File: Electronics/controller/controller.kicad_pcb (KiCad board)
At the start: 2 copper layers, 73.7 x 61 mm, 23 parts, among them P1 POWER, P2 PANEL_1, P3 PANEL_2, P4 DIAL, P5 SWITCH, Q1 FET, U1 LM317T, U2 74HC595, U3 Arduino_Pro_Micro

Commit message: Reworking controller board.
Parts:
- removed P4: DIAL, Connect:bornier3
- removed P5: SWITCH, Connect:bornier2
- added ENC1: Encoder, Cylindric:ALPS_Encoder-EC12E2420404, F.Cu at (66.0, 92.5)
- added SW1: SW_PUSH, Discret:SW_PUSH-12mm, F.Cu at (134.6, 99.1)
- moved C1 90.6 mm to (68.6, 87.6), turned to 90 degrees
- moved C2 83.8 mm to (63.5, 85.1), turned to 270 degrees
- moved LED_DISPLAY1 83.1 mm to (100.3, 99.1), turned to 0 degrees
- moved P1 81.5 mm to (194.8, 82.3)
- moved P2 81.5 mm to (206.2, 82.3)
- moved P3 81.5 mm to (216.4, 82.3)
- moved Q1 81.5 mm to (211.3, 89.9)
- moved R2 81.5 mm to (200.5, 97.5)
- moved R3 81.5 mm to (200.5, 95.0)
- moved U1 81.5 mm to (192.9, 92.4)
- moved R8 67.0 mm to (108.0, 71.1), turned to 180 degrees
- moved R6 65.3 mm to (108.0, 73.7), turned to 180 degrees
- moved R11 63.9 mm to (108.0, 76.2), turned to 180 degrees
- moved R10 63.2 mm to (108.0, 88.9), turned to 180 degrees
- moved R5 63.0 mm to (108.0, 78.7), turned to 180 degrees
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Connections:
- LED_DISPLAY1 pad 1: /D5 -> /D15
- LED_DISPLAY1 pad 2: /D6 -> /D14
- LED_DISPLAY1 pad 6: /D7 -> /D10
- LED_DISPLAY1 pad 8: /D8 -> /D16
- U3 pad 10: /D6 -> (no net)
- U3 pad 11: /D5 -> (no net)
- U3 pad 17: (no net) -> /A0
- U3 pad 8: /D8 -> (no net)
- U3 pad 9: /D7 -> (no net)
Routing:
- net /D8: track 80.6 -> 0.00 mm
- net /D7: track 70.8 -> 0.00 mm
- net /D6: track 56.2 -> 0.00 mm
- net /D5: track 48.3 -> 0.00 mm
- net /D15: track 26.5 -> 56.9 mm
- net Net-(LED_DISPLAY1-Pad3): track 16.9 -> 42.0 mm
- net /A0: track 0.00 -> 22.9 mm
- net Net-(LED_DISPLAY1-Pad16): track 3.59 -> 25.6 mm
- net /D14: track 33.0 -> 51.8 mm
- net Net-(LED_DISPLAY1-Pad15): track 3.59 -> 22.0 mm
- net Net-(LED_DISPLAY1-Pad14): track 3.59 -> 18.4 mm
- net Net-(LED_DISPLAY1-Pad4): track 13.8 -> 26.0 mm
- net Net-(LED_DISPLAY1-Pad13): track 2.54 -> 12.3 mm
- net /D2: track 35.5 -> 28.8 mm
- net Net-(LED_DISPLAY1-Pad5): track 13.7 -> 19.9 mm
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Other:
- board outline removed

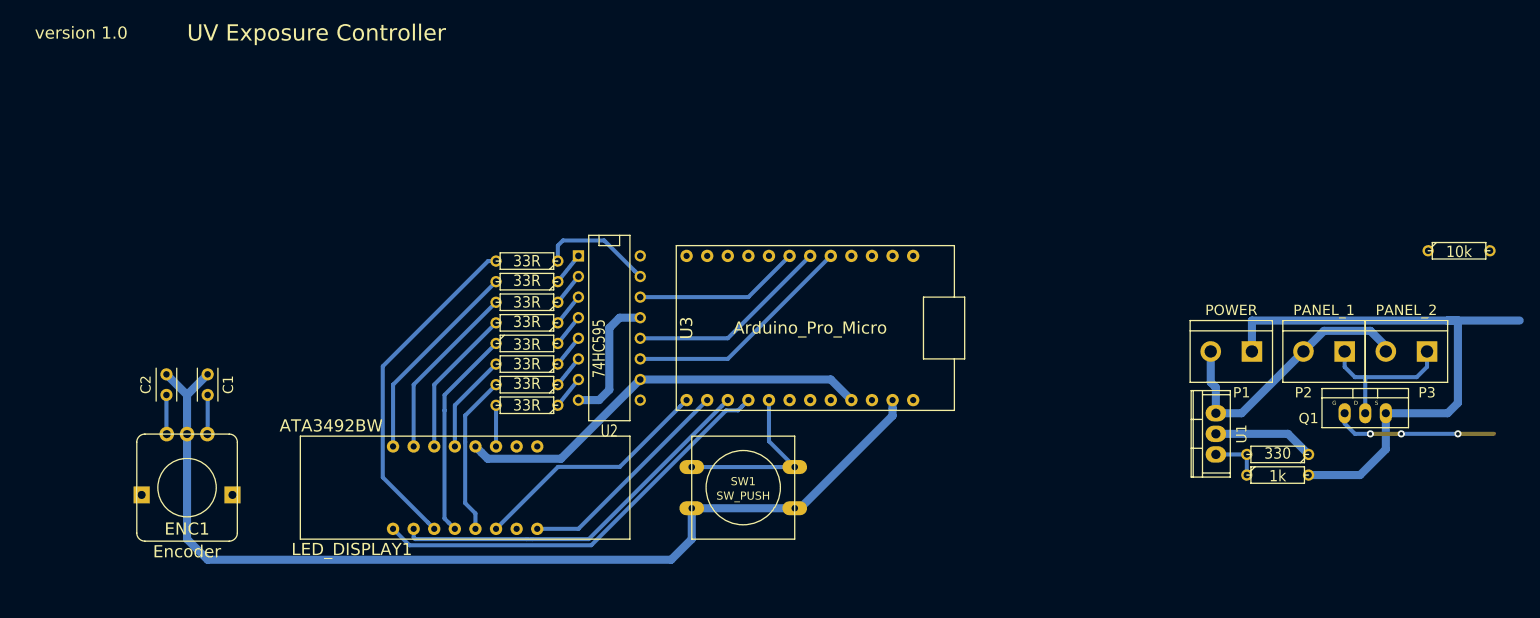
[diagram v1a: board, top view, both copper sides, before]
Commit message: Update with single layout board.
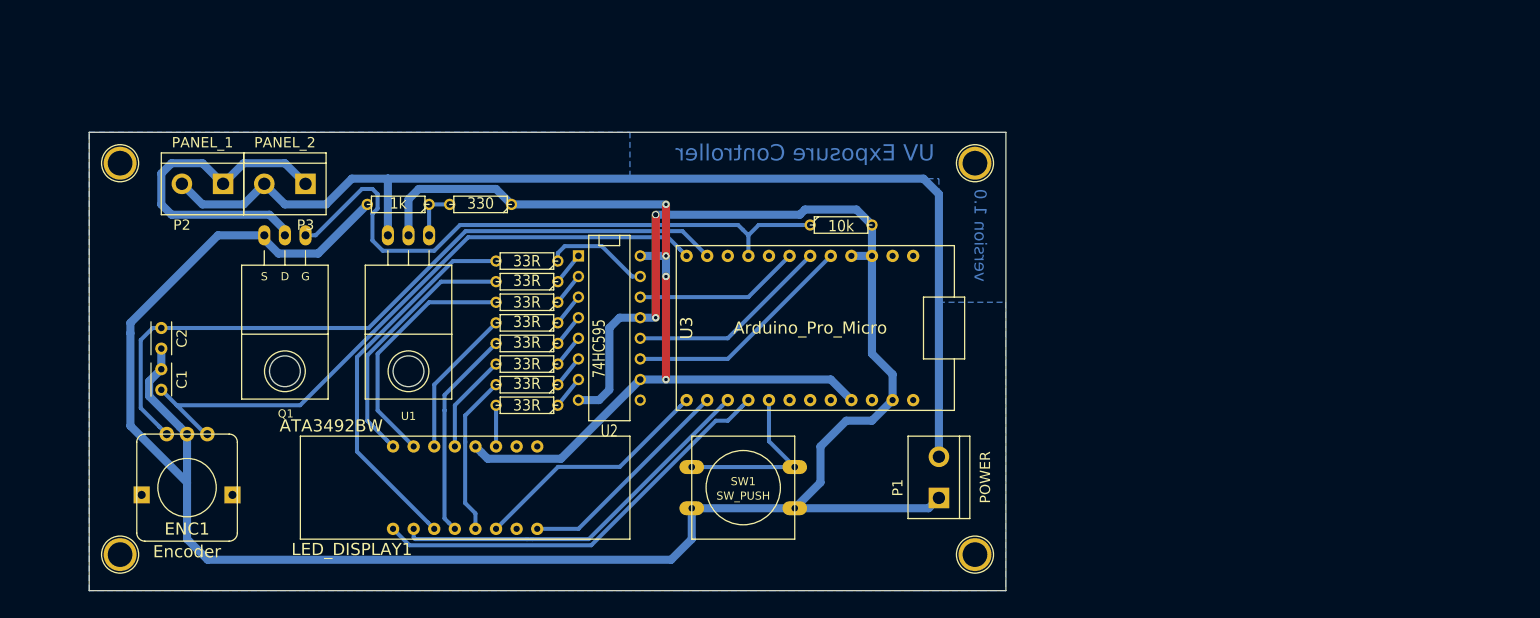
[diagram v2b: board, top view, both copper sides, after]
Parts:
- added 1pin: VAL**, Connect:1pin, F.Cu at (163.2, 59.1)
- added 1pin: VAL**, Connect:1pin, F.Cu at (163.2, 107.3)
- added 1pin: VAL**, Connect:1pin, F.Cu at (57.8, 59.1)
- added 1pin: VAL**, Connect:1pin, F.Cu at (57.8, 107.3)
- Q1: footprint Transistors_TO-220:TO-220_FET-GDS_Vertical -> Transistors_TO-220:TO-220_FET-GDS_Horizontal
- U1: footprint Power_Integrations:TO-220 -> Transistors_TO-220:TO-220_Neutral123_Horizontal
- moved P2 139.8 mm to (67.9, 61.6)
- moved P3 139.8 mm to (78.1, 61.6)
- moved Q1 135.0 mm to (78.1, 67.9), turned to 180 degrees
- moved R2 113.5 mm to (92.1, 64.1), turned to 180 degrees
- moved R3 103.0 mm to (102.2, 64.1)
- moved U1 102.5 mm to (93.3, 67.9), turned to 180 degrees
- moved R4 76.3 mm to (146.7, 66.7)
- moved P1 39.3 mm to (158.8, 97.8), turned to 90 degrees
- moved C1 5.75 mm to (62.9, 87.0)
- moved C2 3.24 mm to (62.9, 81.9), turned to 90 degrees
- turned R1 to 180 degrees
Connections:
- net Net-(P2-Pad1) renamed /12VGND
- C1 pad 1: /D14 -> /D9
- C2 pad 2: /D15 -> /D8
- ENC1 pad A: /D14 -> /D9
- ENC1 pad B: /D15 -> /D8
- Q1 pad G: /D16 -> /D6
- R1 pad 1: Net-(LED_DISPLAY1-Pad4) -> /COL
- R1 pad 2: /COL -> Net-(LED_DISPLAY1-Pad4)
- R4 pad 1: /D16 -> /D6
- U3 pad 11: (no net) -> /D8
- U3 pad 12: (no net) -> /D9
- U3 pad 9: (no net) -> /D6
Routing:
- net +12V: track 34.5 -> 138.5 mm
- net /D8: track 0.00 -> 89.7 mm
- net /D9: track 0.00 -> 80.4 mm
- net /D6: track 0.00 -> 76.9 mm
- net GND: track 215.1 -> 289.2 mm, vias 0 -> 2
- net VCC: track 64.6 -> 114.4 mm, vias 0 -> 4
- net /12VGND: track 19.5 -> 41.8 mm
- net /D16: track 47.7 -> 27.5 mm, vias 3 -> 0
- net Net-(LED_DISPLAY1-Pad15): track 22.0 -> 30.5 mm
- net Net-(LED_DISPLAY1-Pad16): track 25.6 -> 32.2 mm
- net Net-(LED_DISPLAY1-Pad3): track 42.0 -> 47.2 mm
- net /D14: track 51.8 -> 47.0 mm
- net /D15: track 56.9 -> 52.1 mm
- net /D: track 14.2 -> 13.0 mm
- added copper zone on B.Cu, net GND
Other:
- board outline added: 113 x 56.5 mm

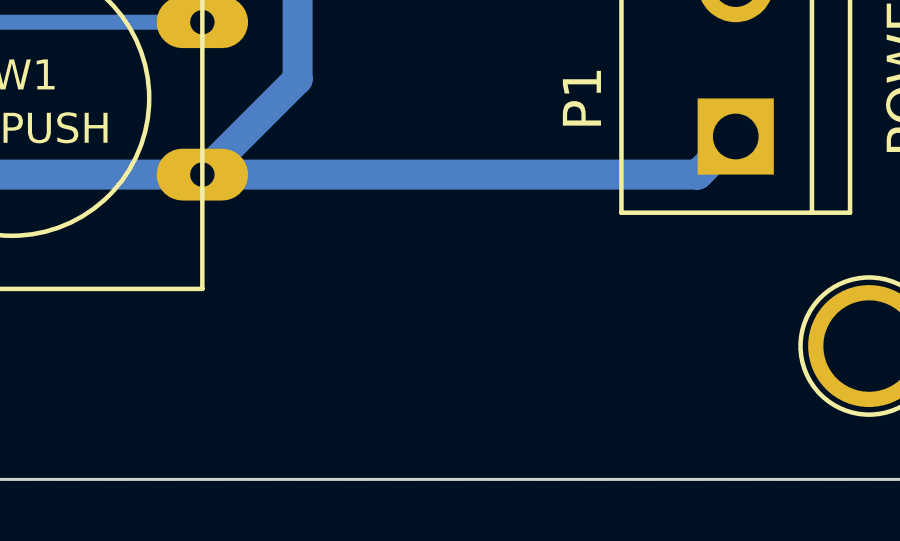
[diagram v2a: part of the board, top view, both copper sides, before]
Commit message: Added the OSHW logo to the controller.
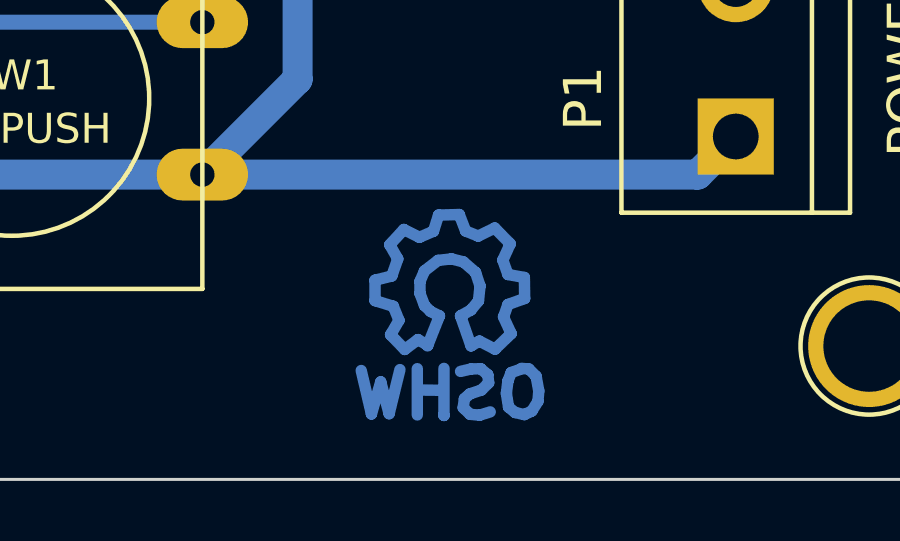
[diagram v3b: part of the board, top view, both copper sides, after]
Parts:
- added Symbol_OSHW-Logo_CopperTop: VAL**, Symbols:Symbol_OSHW-Logo_CopperTop, B.Cu at (149.2, 105.4)

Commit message: Playing with layout.
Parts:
- moved C1 6.02 mm to (68.6, 88.9)
- moved C2 4.49 mm to (63.5, 86.4), turned to 270 degrees
- moved U1 4.26 mm to (89.5, 69.8)
- moved Q1 2.29 mm to (76.8, 69.8)
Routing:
- net /D6: track 76.9 -> 87.6 mm
- net Net-(LED_DISPLAY1-Pad15): track 30.5 -> 22.0 mm
- net /D9: track 80.4 -> 72.2 mm
- net Net-(LED_DISPLAY1-Pad16): track 32.2 -> 25.6 mm
- net Net-(LED_DISPLAY1-Pad3): track 47.2 -> 41.4 mm
- net VCC: track 114.4 -> 117.8 mm
- net Net-(R2-Pad1): track 6.35 -> 9.83 mm
- net +12V: track 138.5 -> 142.0 mm
- net GND: track 289.2 -> 285.8 mm
- net /12VGND: track 41.8 -> 43.2 mm
- net /D8: track 89.7 -> 88.4 mm
- net /D15: track 52.1 -> 52.7 mm

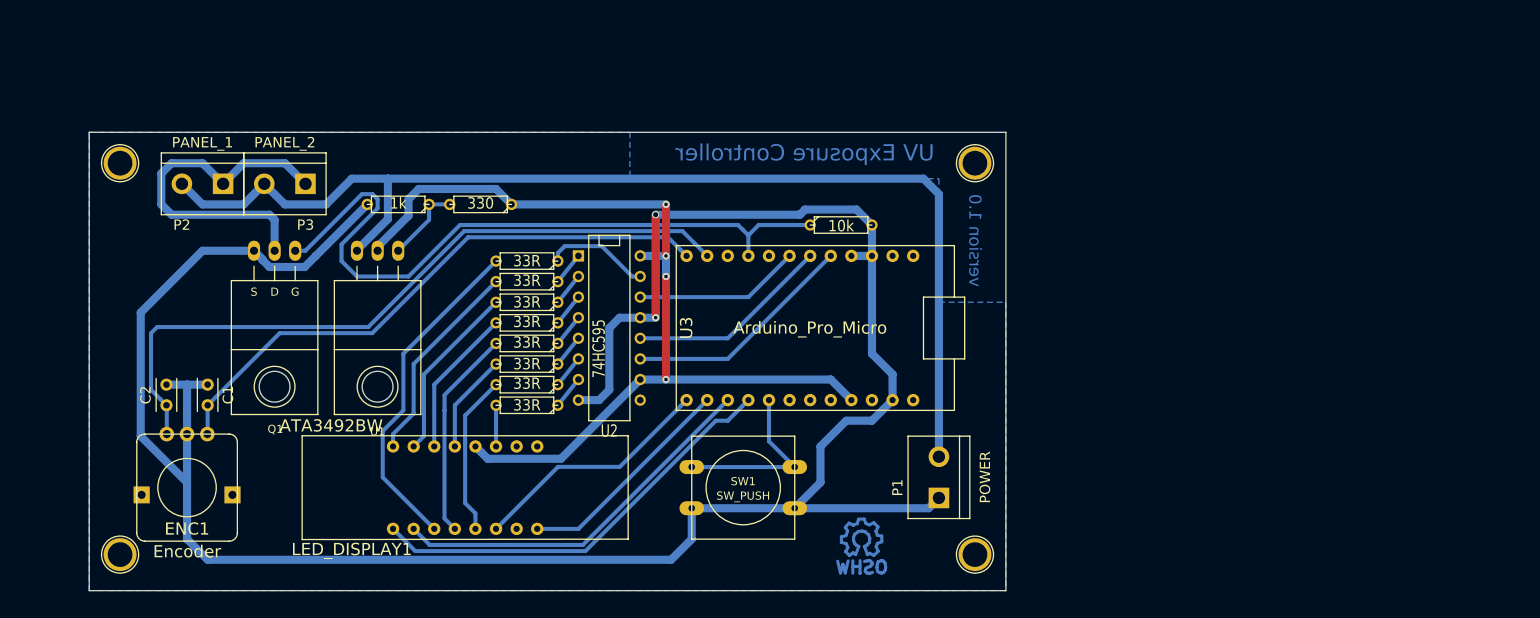
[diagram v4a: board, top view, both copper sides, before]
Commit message: Change a couple of footprints.
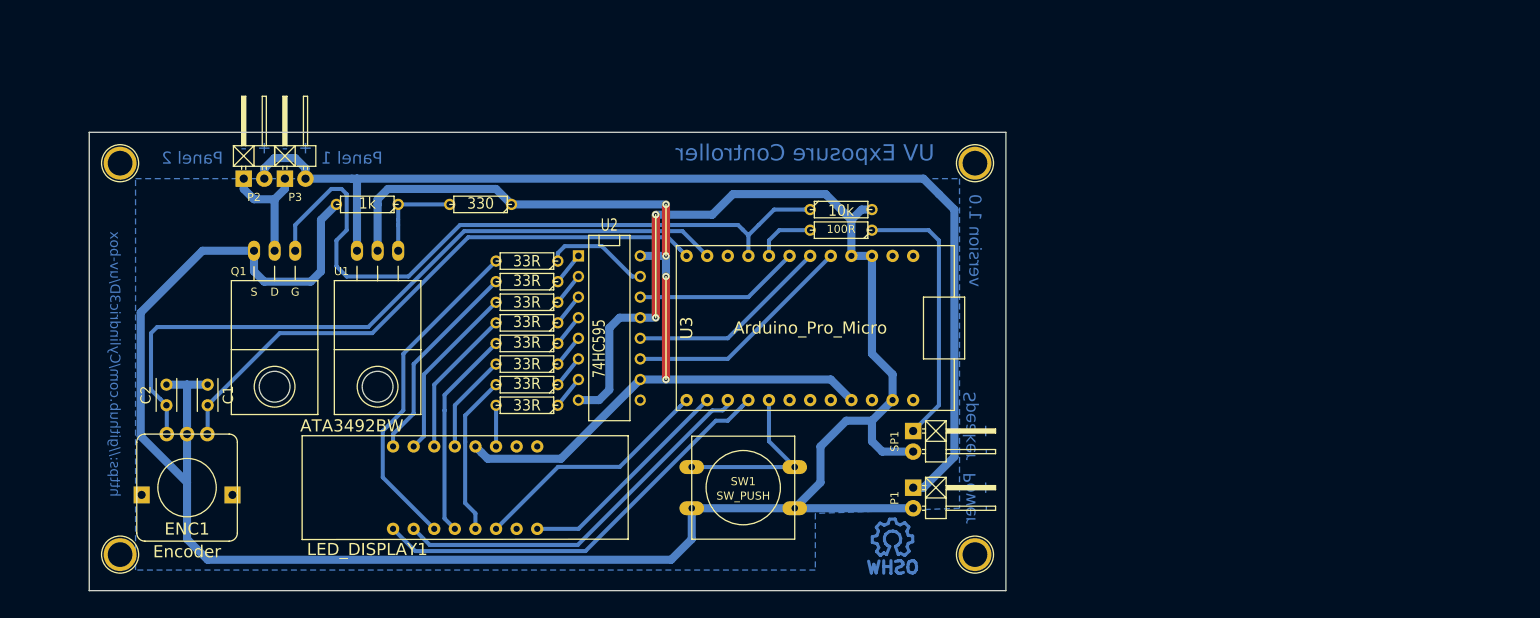
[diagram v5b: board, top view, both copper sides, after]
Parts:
- added R12: 100R, Discret:R3, F.Cu at (146.7, 67.3)
- added SP1: SPEAKER, Pin_Headers:Pin_Header_Angled_1x02, F.Cu at (155.6, 93.3)
- P1, P2, P3: footprint Connect:bornier2 -> Pin_Headers:Pin_Header_Angled_1x02
- moved P2 6.38 mm to (74.3, 61.0), turned to 0 degrees
- moved P1 4.07 mm to (155.6, 100.3), turned to 270 degrees
- moved R2 3.81 mm to (88.3, 64.1)
- moved Symbol_OSHW-Logo_CopperTop 3.81 mm to (153.0, 105.4)
- moved R4 1.91 mm to (146.7, 64.8)
- moved P3 1.42 mm to (79.4, 61.0), turned to 0 degrees
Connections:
- P1 pad 1: GND -> +12V
- P1 pad 2: +12V -> GND
- U3 pad 8: (no net) -> /D5
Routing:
- net Net-(R12-Pad1): track 0.00 -> 33.6 mm
- net /12VGND: track 43.2 -> 15.0 mm
- net GND: track 285.8 -> 295.6 mm
- net /D5: track 0.00 -> 7.51 mm
- net +12V: track 142.0 -> 136.3 mm
- net VCC: track 117.8 -> 120.1 mm
- net Net-(R2-Pad1): track 9.83 -> 12.1 mm
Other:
- board text added: "+"
- board text added: "-"
- board text added: "Panel 1"
- board text added: "Panel 2"
- board text added: "Power"
- board text added: "Speaker"
- board text added: "https://github.com/Cylindric3D/uv-box"
